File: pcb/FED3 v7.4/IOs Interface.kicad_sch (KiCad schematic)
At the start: 29 parts, among them IC1 MC74VHC1GT125, Q2 DMP2035U-7

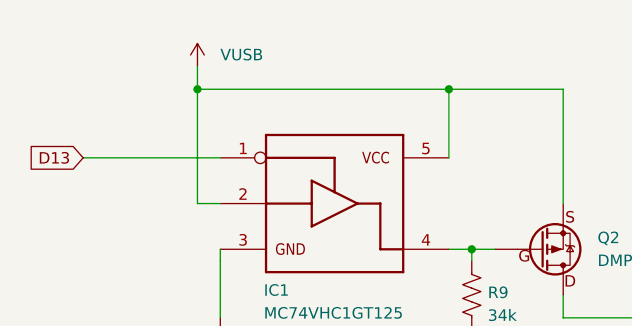
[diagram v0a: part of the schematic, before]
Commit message: v.7.4 - alterações rail power
v.7.4
- modificada estrutura rail power: VUSB apenas para Vcharging
- modificadas Rs de LEDs para diminuir I
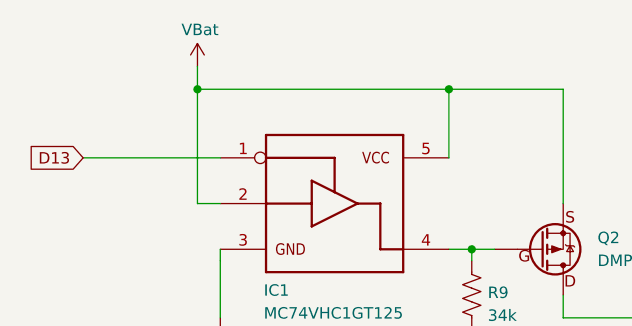
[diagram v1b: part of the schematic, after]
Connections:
- net VUSB renamed VBat
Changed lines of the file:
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@@
-	)
-	(symbol
-		(lib_id "FED3 SymbLib:VUSB")
-		(at 35.56 24.13 0)
-		(unit 1)
-		(exclude_from_sim no)
-		(in_bom yes)
-		(on_board yes)
-		(dnp no)
-		(fields_autoplaced yes)
-		(property "Reference" "#PWR08"
-			(at 35.56 27.94 0)
-			(effects
-				(font
-					(size 1.27 1.27)
-				)
-				(justify bottom)
-				(hide yes)
-			)
-		)
-		(property "Value" "VUSB"
-			(at 38.1 22.8599 0)
-			(effects
-				(font
-					(size 1.27 1.27)
-				)
-				(justify left)
-			)
-		)
-		(property "Footprint" ""
-			(at 35.56 24.13 0)
-			(effects
-				(font
-					(size 1.27 1.27)
-				)
-				(hide yes)
-			)
-		)
-		(property "Datasheet" ""
-			(at 35.56 24.13 0)
-			(effects
-				(font
-					(size 1.27 1.27)
-				)
-				(hide yes)
-			)
-		)
-		(property "Description" "Power symbol creates a global label with name \"VUSB\""
-			(at 35.56 24.13 0)
-			(effects
-				(font
-					(size 1.27 1.27)
-				)
-				(hide yes)
-			)
-		)
-		(pin "1"
-		)
-		(instances
-			(project "FED3_v7.3"
-				(path "/2ba63f12-2fcd-4471-9636-2762cde37de8/91f92fff-cc86-4ce2-a671-c31760f8020c"
-					(reference "#PWR08")
-					(unit 1)
-				)
-			)
-		)
 	)
 	(symbol
@@
 					(unit 1)
 				)
+			)
+		)
+	)
+	(symbol
+		(lib_id "FED3 SymbLib:V_Batt")
+		(at 35.56 24.13 0)
+		(unit 1)
+		(exclude_from_sim no)
+		(in_bom yes)
+		(on_board yes)
+		(dnp no)
+		(property "Reference" "#PWR07"
+			(at 35.56 27.94 0)
+			(effects
+				(font
+					(size 1.27 1.27)
+				)
+				(justify bottom)
+				(hide yes)
+			)
+		)
+		(property "Value" "VBat"
+			(at 33.782 20.066 0)
+			(effects
+				(font
+					(size 1.27 1.27)
+				)
+				(justify left)
+			)
+		)
+		(property "Footprint" ""
+			(at 35.56 24.13 0)
+			(effects
+				(font
+					(size 1.27 1.27)
+				)
+				(hide yes)
+			)
+		)
+		(property "Datasheet" ""
+			(at 35.56 24.13 0)
+			(effects
+				(font
+					(size 1.27 1.27)
+				)
+				(hide yes)
+			)
+		)
+		(property "Description" "Power symbol creates a global label with name \"V_Batt\""
+			(at 35.56 24.13 0)
+			(effects
+				(font
+					(size 1.27 1.27)
+				)
+				(hide yes)
+			)
+		)
+		(pin "1"
+		)
+		(instances
+			(project "FED3"
+				(path "/2ba63f12-2fcd-4471-9636-2762cde37de8/91f92fff-cc86-4ce2-a671-c31760f8020c"
+					(reference "#PWR07")
+					(unit 1)
+				)
